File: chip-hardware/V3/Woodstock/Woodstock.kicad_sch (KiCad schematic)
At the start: 8 parts

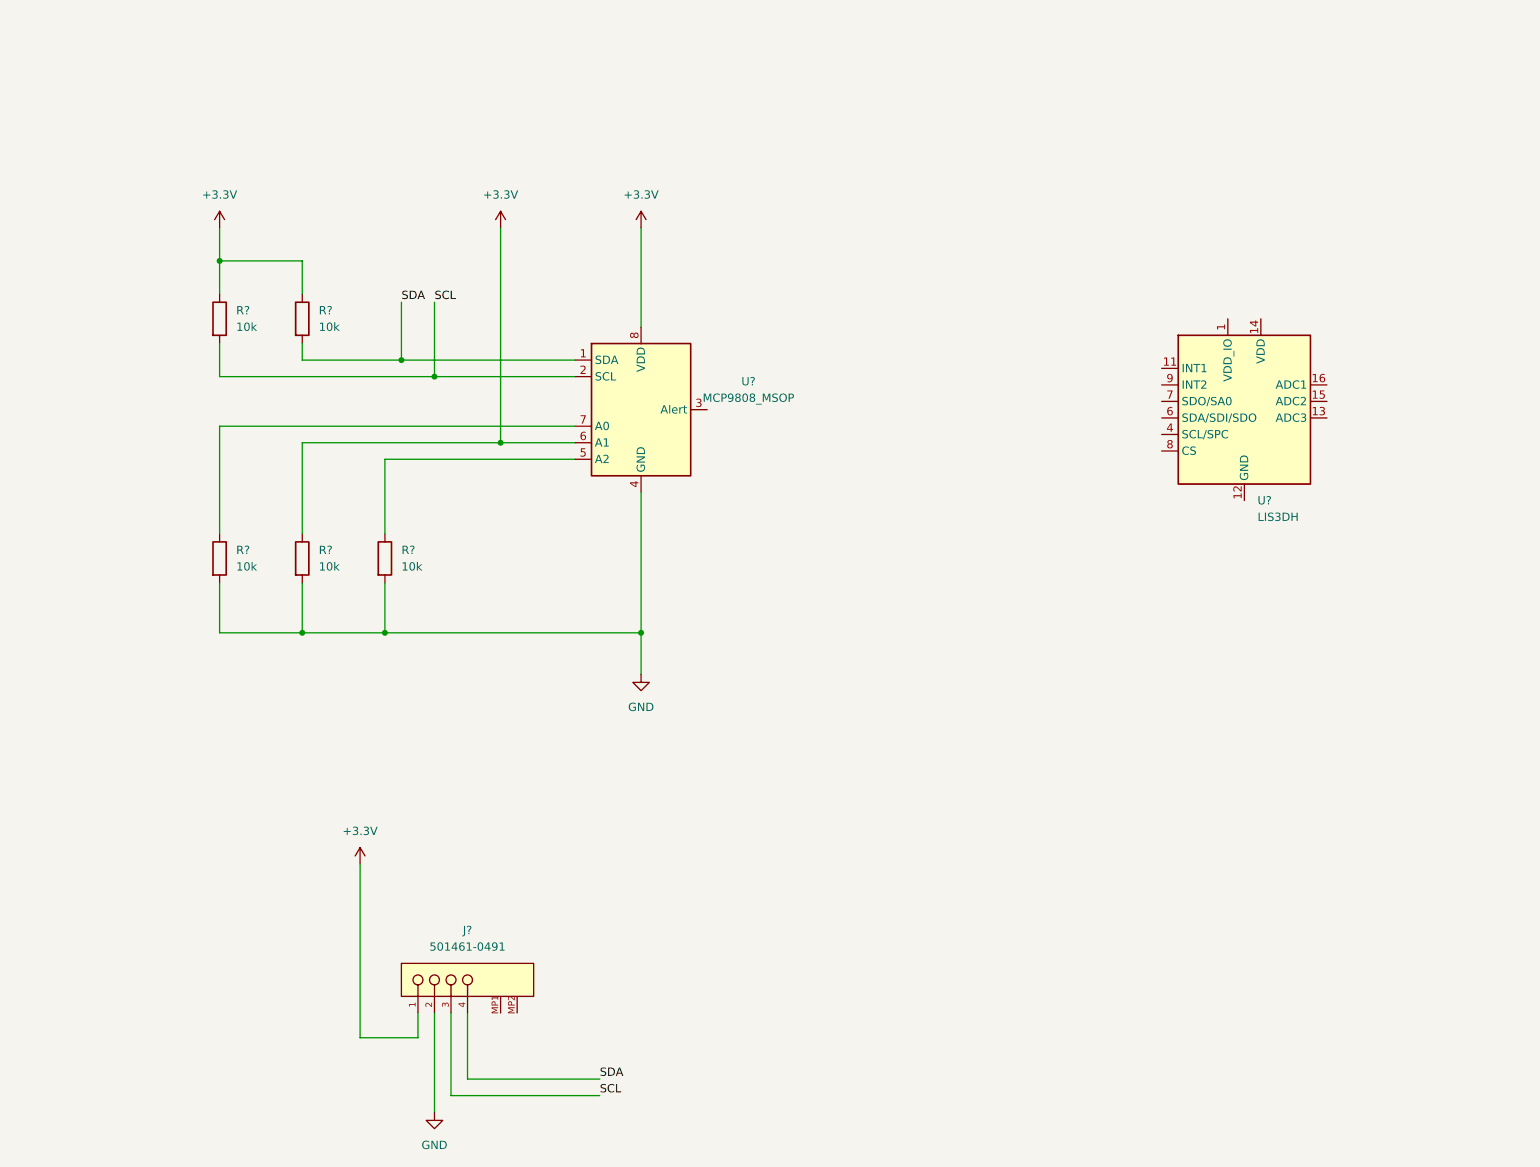
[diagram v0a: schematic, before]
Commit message: Added pwr flag
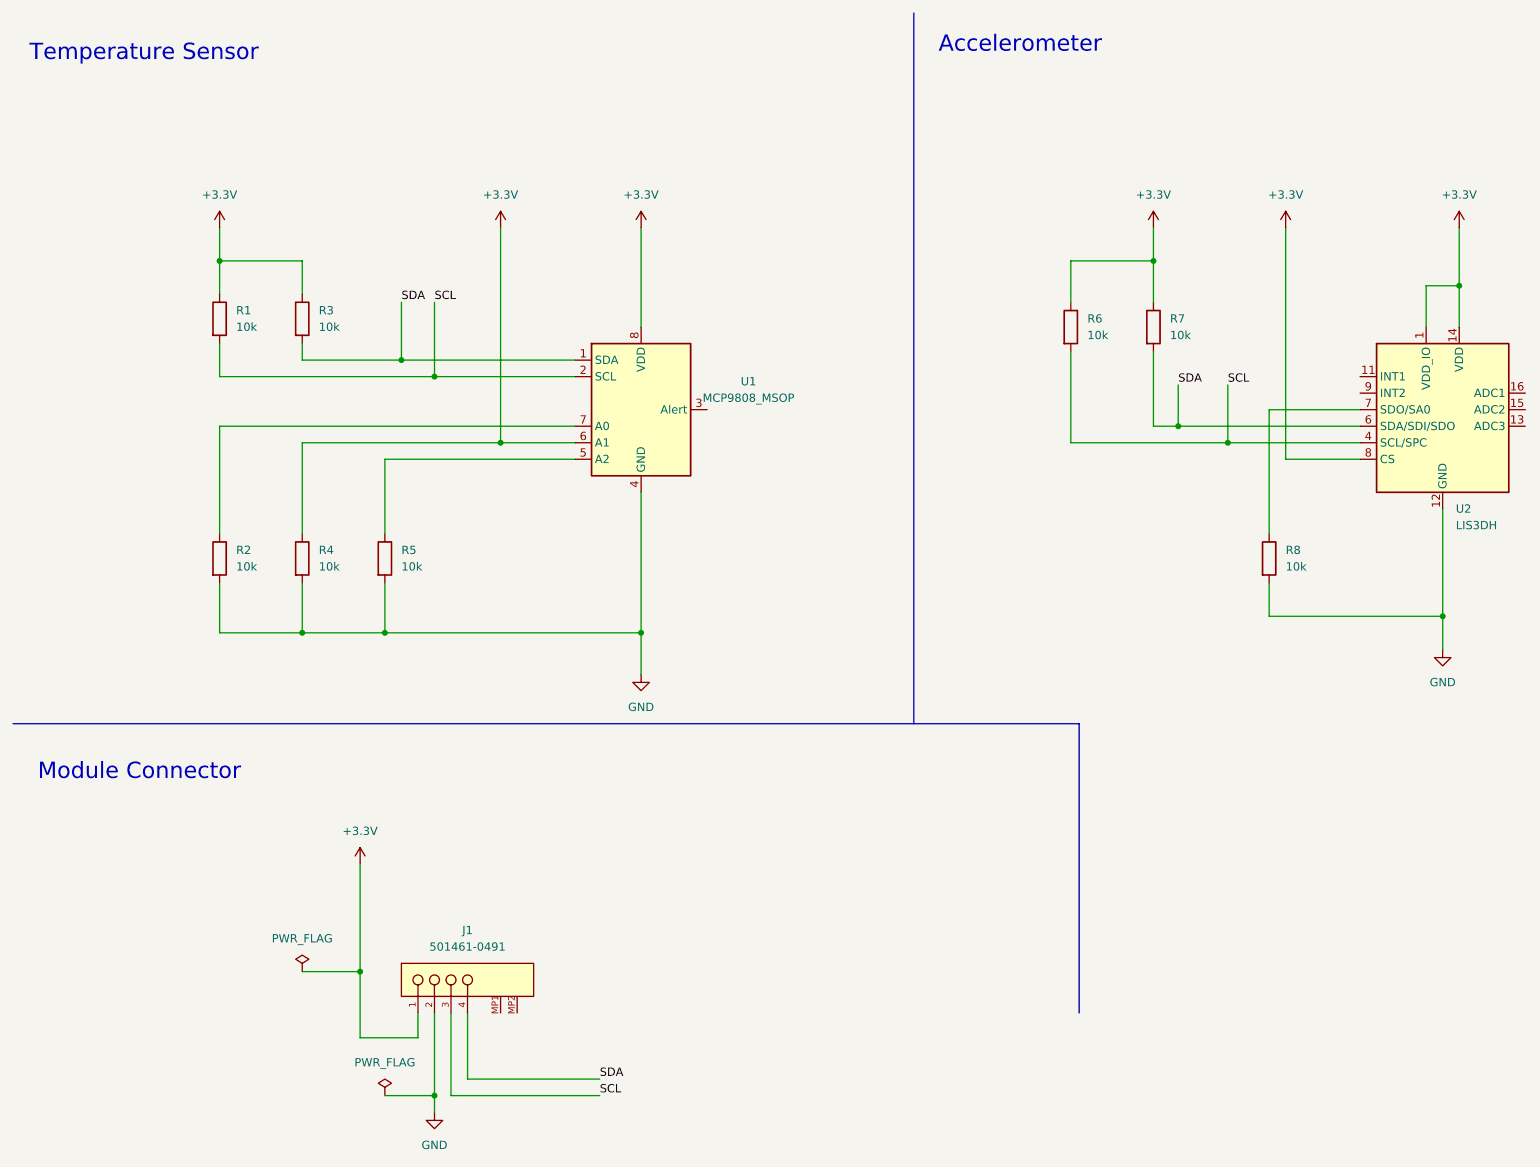
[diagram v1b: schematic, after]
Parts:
- added R6, R7, R8: 10k, symbol Device:R
- gave numbers to parts that had none: 8
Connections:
- net +3V3: now also U2.1 (VDD_IO), U2.14 (VDD), U2.8 (CS), R6.1, R7.1
- net GND: now also U2.10 (GND), U2.12 (GND), U2.5 (GND), R8.2
- net SCL: now also U2.4 (SCL/SPC), R6.2
- net SDA: now also U2.6 (SDA/SDI/SDO), R7.2
- net at U2.7 (SDO/SA0): now also R8.1
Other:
- note added: "Accelerometer"
- note added: "Module Connector"
- note added: "Temperature Sensor"
- moved on the sheet: U2

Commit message: All parts associated correctly and assigned to parts
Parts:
- J1: footprint Molex-501461-0491-* -> 5014610491:Molex-501461-0491-Manufacturer_Recommended
- R1, R2, R3, R4, R5, R6, R7, R8: footprint (none) -> Resistor_SMD:R_0603_1608Metric_Pad0.98x0.95mm_HandSolder
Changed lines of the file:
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@@
       (effects (font (size 1.27 1.27)) (justify left))
     )
-    (property "Footprint" "" (id 2) (at 173.482 60.96 90)
+    (property "Footprint" "Resistor_SMD:R_0603_1608Metric_Pad0.98x0.95mm_HandSolder" (id 2) (at 173.482 60.96 90)
       (effects (font (size 1.27 1.27)) hide)
     )
@@
       (effects (font (size 1.27 1.27)) (justify left))
     )
-    (property "Footprint" "" (id 2) (at 68.072 96.52 90)
+    (property "Footprint" "Resistor_SMD:R_0603_1608Metric_Pad0.98x0.95mm_HandSolder" (id 2) (at 68.072 96.52 90)
       (effects (font (size 1.27 1.27)) hide)
     )
@@
       (effects (font (size 1.27 1.27)) (justify left))
     )
-    (property "Footprint" "" (id 2) (at 55.372 96.52 90)
+    (property "Footprint" "Resistor_SMD:R_0603_1608Metric_Pad0.98x0.95mm_HandSolder" (id 2) (at 55.372 96.52 90)
       (effects (font (size 1.27 1.27)) hide)
     )
@@
       (effects (font (size 1.27 1.27)) (justify left))
     )
-    (property "Footprint" "" (id 2) (at 42.672 96.52 90)
+    (property "Footprint" "Resistor_SMD:R_0603_1608Metric_Pad0.98x0.95mm_HandSolder" (id 2) (at 42.672 96.52 90)
       (effects (font (size 1.27 1.27)) hide)
     )
@@
       (effects (font (size 1.27 1.27)) (justify left))
     )
-    (property "Footprint" "" (id 2) (at 42.672 59.69 90)
+    (property "Footprint" "Resistor_SMD:R_0603_1608Metric_Pad0.98x0.95mm_HandSolder" (id 2) (at 42.672 59.69 90)
       (effects (font (size 1.27 1.27)) hide)
     )
@@
       (effects (font (size 1.27 1.27)) (justify left))
     )
-    (property "Footprint" "" (id 2) (at 186.182 60.96 90)
+    (property "Footprint" "Resistor_SMD:R_0603_1608Metric_Pad0.98x0.95mm_HandSolder" (id 2) (at 186.182 60.96 90)
       (effects (font (size 1.27 1.27)) hide)
     )
@@
       (effects (font (size 1.27 1.27)) (justify left))
     )
-    (property "Footprint" "" (id 2) (at 55.372 59.69 90)
+    (property "Footprint" "Resistor_SMD:R_0603_1608Metric_Pad0.98x0.95mm_HandSolder" (id 2) (at 55.372 59.69 90)
       (effects (font (size 1.27 1.27)) hide)
     )
@@
     (property "Reference" "J1" (id 0) (at 82.55 153.67 0))
     (property "Value" "501461-0491" (id 1) (at 82.55 156.21 0))
-    (property "Footprint" "Molex-501461-0491-*" (id 2) (at 74.93 151.13 0)
+    (property "Footprint" "5014610491:Molex-501461-0491-Manufacturer_Recommended" (id 2) (at 74.93 151.13 0)
       (effects (font (size 1.27 1.27)) (justify left) hide)
     )
@@
       (effects (font (size 1.27 1.27)) (justify left))
     )
-    (property "Footprint" "" (id 2) (at 203.962 96.52 90)
+    (property "Footprint" "Resistor_SMD:R_0603_1608Metric_Pad0.98x0.95mm_HandSolder" (id 2) (at 203.962 96.52 90)
       (effects (font (size 1.27 1.27)) hide)
     )
@@
     )
     (path "/7813914e-b620-4aec-b413-d4610daa8307"
-      (reference "J1") (unit 1) (value "501461-0491") (footprint "Molex-501461-0491-*")
+      (reference "J1") (unit 1) (value "501461-0491") (footprint "5014610491:Molex-501461-0491-Manufacturer_Recommended")
     )
     (path "/308027e9-ee4f-43ba-b32e-c7d56fa7200c"
-      (reference "R1") (unit 1) (value "10k") (footprint "")
+      (reference "R1") (unit 1) (value "10k") (footprint "Resistor_SMD:R_0603_1608Metric_Pad0.98x0.95mm_HandSolder")
     )
     (path "/220b09bc-452d-473c-8105-3138f1069ef5"
-      (reference "R2") (unit 1) (value "10k") (footprint "")
+      (reference "R2") (unit 1) (value "10k") (footprint "Resistor_SMD:R_0603_1608Metric_Pad0.98x0.95mm_HandSolder")
     )
     (path "/75c0ba43-bcb2-42b6-b1df-717c01eb63ff"
-      (reference "R3") (unit 1) (value "10k") (footprint "")
+      (reference "R3") (unit 1) (value "10k") (footprint "Resistor_SMD:R_0603_1608Metric_Pad0.98x0.95mm_HandSolder")
     )
     (path "/1dd88aea-b250-46d6-93b0-9bbc0ac4d7cc"
-      (reference "R4") (unit 1) (value "10k") (footprint "")
+      (reference "R4") (unit 1) (value "10k") (footprint "Resistor_SMD:R_0603_1608Metric_Pad0.98x0.95mm_HandSolder")
     )
     (path "/125c6a85-77b3-464d-afa9-485763f4c7a9"
-      (reference "R5") (unit 1) (value "10k") (footprint "")
+      (reference "R5") (unit 1) (value "10k") (footprint "Resistor_SMD:R_0603_1608Metric_Pad0.98x0.95mm_HandSolder")
     )
     (path "/0ecf933e-65d8-4a95-9dfc-294181bec934"
-      (reference "R6") (unit 1) (value "10k") (footprint "")
+      (reference "R6") (unit 1) (value "10k") (footprint "Resistor_SMD:R_0603_1608Metric_Pad0.98x0.95mm_HandSolder")
     )
     (path "/56f72fbb-34c4-4c32-9ed1-180b74618c6e"
-      (reference "R7") (unit 1) (value "10k") (footprint "")
+      (reference "R7") (unit 1) (value "10k") (footprint "Resistor_SMD:R_0603_1608Metric_Pad0.98x0.95mm_HandSolder")
     )
     (path "/842a3f4f-2752-4079-a0ce-1a06e82c67ff"
-      (reference "R8") (unit 1) (value "10k") (footprint "")
+      (reference "R8") (unit 1) (value "10k") (footprint "Resistor_SMD:R_0603_1608Metric_Pad0.98x0.95mm_HandSolder")
     )
     (path "/7871d994-27c3-4ca4-848f-782f09d0ed0a"
